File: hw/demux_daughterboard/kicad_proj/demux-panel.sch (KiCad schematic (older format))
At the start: 28 parts, among them P1 CONN_5, P10 CONN_2, P2 CONN_8X2, P3 CONN_8X2, P4 CONN_2, P5 CONN_5, P6 CONN_2, P7 CONN_8X2, P8 CONN_8X2, P9 CONN_3X2

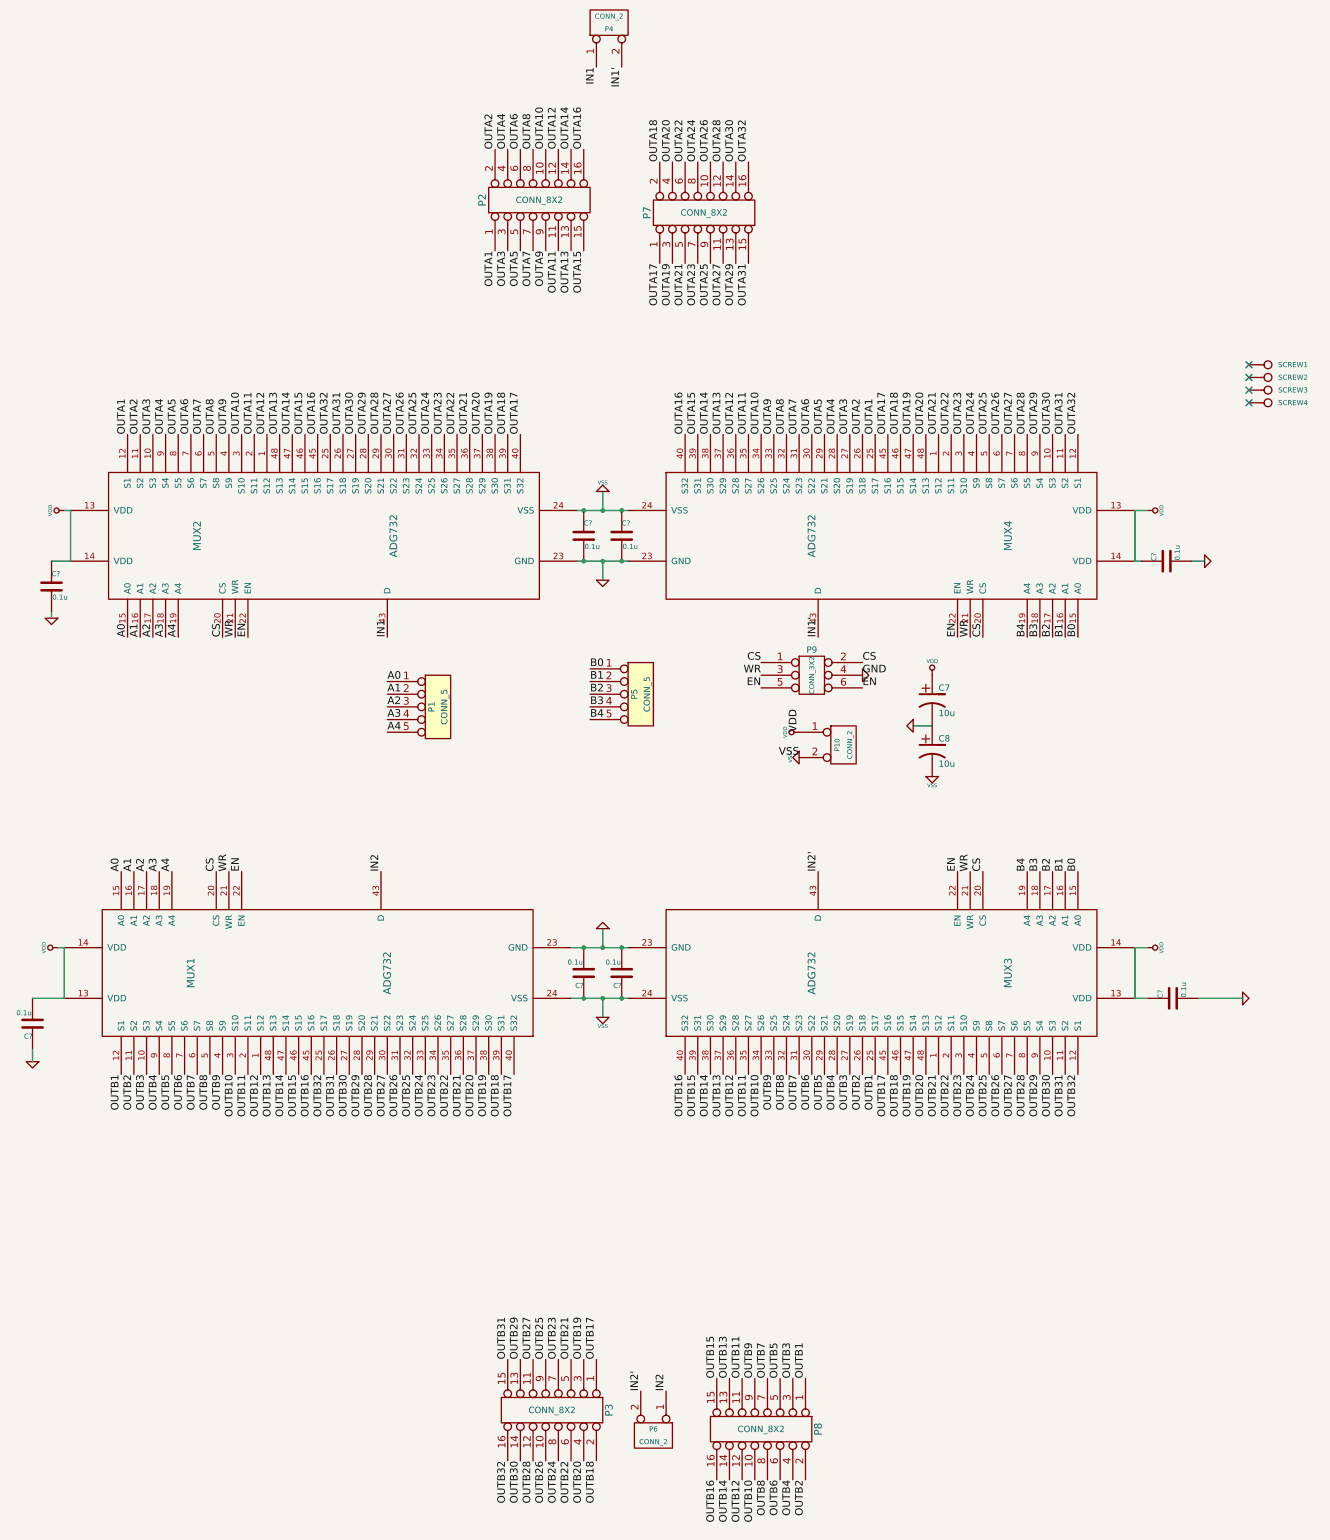
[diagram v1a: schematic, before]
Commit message: Finished daughterboard pcb with fusion pcb constraints, TODO: silkscreen
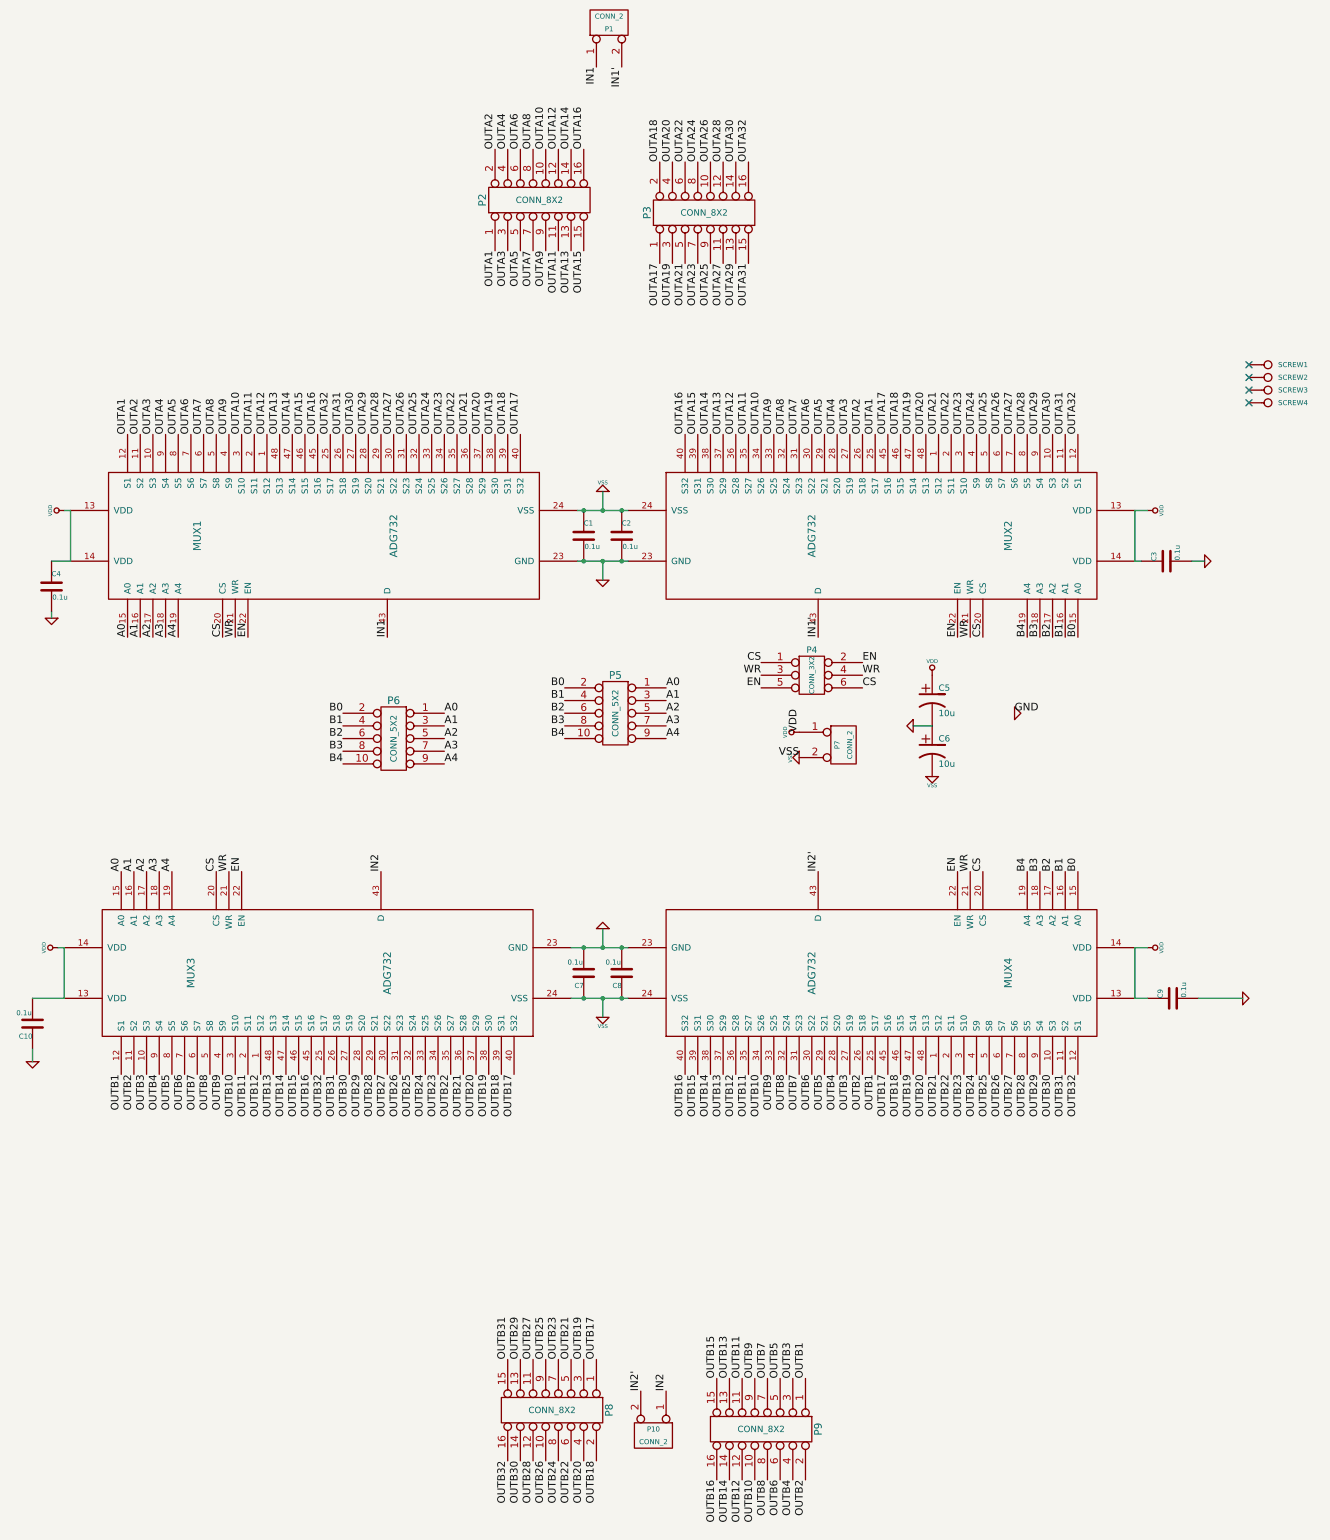
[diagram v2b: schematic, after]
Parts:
- removed P1, P5: CONN_5, symbol CONN_5
- added P5, P6: CONN_5X2, symbol CONN_5X2
- gave numbers to parts that had none: 8
- renumbered C7 to C5, C8 to C6, MUX2 to MUX1, MUX4 to MUX2, MUX1 to MUX3, MUX3 to MUX4, P4 to P1, P6 to P10, P7 to P3, P9 to P4, P10 to P7, P3 to P8, P8 to P9
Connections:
- net A0: now also P5.1, P6.1
- net A1: now also P5.3, P6.3
- net A2: now also P5.5, P6.5
- net A3: now also P5.7, P6.7
- net A4: now also P5.9, P6.9
- net B0: now also P5.2, P6.2
- net B1: now also P5.4, P6.4
- net B2: now also P5.6, P6.6
- net B3: now also P5.8, P6.8
- net B4: now also P5.10, P6.10
- net CS: now also P4.6; no longer P4.2
- net EN: now also P4.2; no longer P4.6
- net GND: no longer P4.4
- net WR: now also P4.4
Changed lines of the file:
@@
 LIBS:demuxcomplib
 LIBS:device
+LIBS:conn
 LIBS:demux-panel-cache
 EELAYER 24 0
@@
 Comment4 ""
 $EndDescr
-Text Label 5050 3150 0    60   ~ 0
+Text Label 3100 3500 2    60   ~ 0
 B0
 $Comp
@@
 $EndComp
 $Comp
-L CP1 C8
+L CP1 C6
 U 1 1 53239D33
 P 7750 3800
-F 0 "C8" H 7800 3900 50  0000 L CNN
+F 0 "C6" H 7800 3900 50  0000 L CNN
 F 1 "10u" H 7800 3700 50  0000 L CNN
 F 2 "" H 7750 3800 60  0001 C CNN
@@
 $EndComp
 $Comp
-L CP1 C7
+L CP1 C5
 U 1 1 53239D39
 P 7750 3400
-F 0 "C7" H 7800 3500 50  0000 L CNN
+F 0 "C5" H 7800 3500 50  0000 L CNN
 F 1 "10u" H 7800 3300 50  0000 L CNN
 F 2 "" H 7750 3400 60  0001 C CNN
@@
 L GND #PWR05
 U 1 1 53239D45
-P 7200 3200
-F 0 "#PWR05" H 7200 3200 30  0001 C CNN
-F 1 "GND" H 7200 3130 30  0001 C CNN
-F 2 "" H 7200 3200 60  0001 C CNN
-F 3 "" H 7200 3200 60  0001 C CNN
-	1    7200 3200
+P 8400 3500
+F 0 "#PWR05" H 8400 3500 30  0001 C CNN
+F 1 "GND" H 8400 3430 30  0001 C CNN
+F 2 "" H 8400 3500 60  0001 C CNN
+F 3 "" H 8400 3500 60  0001 C CNN
+	1    8400 3500
 	0    -1   -1   0
 $EndComp
@@
 	0    -1   -1   0
 $EndComp
-Text Label 7200 3200 0    60   ~ 0
+Text Label 8400 3500 0    60   ~ 0
 GND
 Text Label 6700 3850 2    60   ~ 0
@@
 Text Label 6400 3300 2    60   ~ 0
 EN
-Text Label 5050 3550 0    60   ~ 0
+Text Label 3100 3900 2    60   ~ 0
 B4
-Text Label 5050 3450 0    60   ~ 0
+Text Label 3100 3800 2    60   ~ 0
 B3
-Text Label 5050 3350 0    60   ~ 0
+Text Label 3100 3700 2    60   ~ 0
 B2
-Text Label 5050 3250 0    60   ~ 0
+Text Label 3100 3600 2    60   ~ 0
 B1
-Text Label 3450 3650 0    60   ~ 0
+Text Label 3900 3900 0    60   ~ 0
 A4
-Text Label 3450 3550 0    60   ~ 0
+Text Label 3900 3800 0    60   ~ 0
 A3
-Text Label 3450 3450 0    60   ~ 0
+Text Label 3900 3700 0    60   ~ 0
 A2
-Text Label 3450 3350 0    60   ~ 0
+Text Label 3900 3600 0    60   ~ 0
 A1
-Text Label 3450 3250 0    60   ~ 0
-A0
-$Comp
-L CONN_5 P5
-U 1 1 53239D66
-P 5450 3350
-F 0 "P5" V 5400 3350 50  0000 C CNN
-F 1 "CONN_5" V 5500 3350 50  0000 C CNN
-F 2 "" H 5450 3350 60  0001 C CNN
-F 3 "" H 5450 3350 60  0001 C CNN
-	1    5450 3350
-	1    0    0    -1
-$EndComp
-$Comp
-L CONN_5 P1
-U 1 1 53239D6C
-P 3850 3450
-F 0 "P1" V 3800 3450 50  0000 C CNN
-F 1 "CONN_5" V 3900 3450 50  0000 C CNN
-F 2 "" H 3850 3450 60  0001 C CNN
-F 3 "" H 3850 3450 60  0001 C CNN
-	1    3850 3450
-	1    0    0    -1
-$EndComp
 $Comp
 L CONN_1 SCREW4
@@
 $EndComp
 $Comp
-L ADG732 MUX1
+L ADG732 MUX3
 U 1 1 53239EC2
 P 2900 5550
-F 0 "MUX1" H 2900 6550 60  0000 C CNN
+F 0 "MUX3" H 2900 6550 60  0000 C CNN
 F 1 "ADG732" H 2900 5000 60  0000 C CNN
 F 2 "" H 2900 5550 60  0001 C CNN
@@
 $EndComp
 $Comp
-L ADG732 MUX2
+L ADG732 MUX1
 U 1 1 53239EC8
 P 2950 2100
-F 0 "MUX2" H 2950 3100 60  0000 C CNN
+F 0 "MUX1" H 2950 3100 60  0000 C CNN
 F 1 "ADG732" H 2950 1550 60  0000 C CNN
 F 2 "" H 2950 2100 60  0001 C CNN
@@
 $EndComp
 $Comp
-L ADG732 MUX4
+L ADG732 MUX2
 U 1 1 53239ECE
 P 7350 2100
-F 0 "MUX4" H 7350 3100 60  0000 C CNN
+F 0 "MUX2" H 7350 3100 60  0000 C CNN
 F 1 "ADG732" H 7350 1550 60  0000 C CNN
 F 2 "" H 7350 2100 60  0001 C CNN
@@
 $EndComp
 $Comp
-L CONN_3X2 P9
+L CONN_3X2 P4
 U 1 1 53239FB0
 P 6800 3250
-F 0 "P9" H 6800 3500 50  0000 C CNN
+F 0 "P4" H 6800 3500 50  0000 C CNN
 F 1 "CONN_3X2" V 6800 3300 40  0000 C CNN
 F 2 "" H 6800 3250 60  0000 C CNN
@@
 	1    0    0    -1
 $EndComp
+Text Label 7200 3300 0    60   ~ 0
+CS
 Text Label 7200 3100 0    60   ~ 0
-CS
-Text Label 7200 3300 0    60   ~ 0
 EN
 $Comp
-L CONN_2 P10
+L CONN_2 P7
 U 1 1 53239FDE
 P 7050 3750
-F 0 "P10" V 7000 3750 40  0000 C CNN
+F 0 "P7" V 7000 3750 40  0000 C CNN
 F 1 "CONN_2" V 7100 3750 40  0000 C CNN
 F 2 "" H 7050 3750 60  0000 C CNN
@@
 $EndComp
 $Comp
-L CONN_8X2 P7
+L CONN_8X2 P3
 U 1 1 5323C0BE
 P 5950 -450
-F 0 "P7" H 5950 0   60  0000 C CNN
+F 0 "P3" H 5950 0   60  0000 C CNN
 F 1 "CONN_8X2" V 5950 -450 50  0000 C CNN
 F 2 "" H 5950 -450 60  0000 C CNN
@@
 OUTA32
 $Comp
-L CONN_2 P4
+L CONN_2 P1
 U 1 1 5323C58F
 P 5200 -1950
-F 0 "P4" V 5150 -1950 40  0000 C CNN
+F 0 "P1" V 5150 -1950 40  0000 C CNN
 F 1 "CONN_2" V 5250 -1950 40  0000 C CNN
 F 2 "" H 5200 -1950 60  0000 C CNN
@@
 IN1'
 $Comp
-L CONN_8X2 P8
+L CONN_8X2 P9
 U 1 1 5323C6F0
 P 6400 9150
-F 0 "P8" H 6400 9600 60  0000 C CNN
+F 0 "P9" H 6400 9600 60  0000 C CNN
 F 1 "CONN_8X2" V 6400 9150 50  0000 C CNN
 F 2 "" H 6400 9150 60  0000 C CNN
@@
 $EndComp
 $Comp
-L CONN_8X2 P3
+L CONN_8X2 P8
 U 1 1 5323C6F6
 P 4750 9000
-F 0 "P3" H 4750 9450 60  0000 C CNN
+F 0 "P8" H 4750 9450 60  0000 C CNN
 F 1 "CONN_8X2" V 4750 9000 50  0000 C CNN
 F 2 "" H 4750 9000 60  0000 C CNN
@@
 OUTB16
 $Comp
-L CONN_2 P6
+L CONN_2 P10
 U 1 1 5323C787
 P 5550 9200
-F 0 "P6" V 5500 9200 40  0000 C CNN
+F 0 "P10" V 5500 9200 40  0000 C CNN
 F 1 "CONN_2" V 5600 9200 40  0000 C CNN
 F 2 "" H 5550 9200 60  0000 C CNN
@@
 Connection ~ 5000 5750
 $Comp
-L ADG732 MUX3
+L ADG732 MUX4
 U 1 1 53239EBC
 P 7350 5550
-F 0 "MUX3" H 7350 6550 60  0000 C CNN
+F 0 "MUX4" H 7350 6550 60  0000 C CNN
 F 1 "ADG732" H 7350 5000 60  0000 C CNN
 F 2 "" H 7350 5550 60  0001 C CNN
@@
 	650  6150 650  6250
 $Comp
-L C C?
+L C C1
 U 1 1 5323D5A7
 P 5000 2100
-F 0 "C?" H 5000 2200 40  0000 L CNN
+F 0 "C1" H 5000 2200 40  0000 L CNN
 F 1 "0.1u" H 5006 2015 40  0000 L CNN
 F 2 "" H 5038 1950 30  0000 C CNN
@@
 $EndComp
 $Comp
-L C C?
+L C C2
 U 1 1 5323D5D2
 P 5300 2100
-F 0 "C?" H 5300 2200 40  0000 L CNN
+F 0 "C2" H 5300 2200 40  0000 L CNN
 F 1 "0.1u" H 5306 2015 40  0000 L CNN
 F 2 "" H 5338 1950 30  0000 C CNN
@@
 $EndComp
 $Comp
-L C C?
+L C C4
 U 1 1 5323D5D8
 P 800 2500
-F 0 "C?" H 800 2600 40  0000 L CNN
+F 0 "C4" H 800 2600 40  0000 L CNN
 F 1 "0.1u" H 806 2415 40  0000 L CNN
 F 2 "" H 838 2350 30  0000 C CNN
@@
 $EndComp
 $Comp
-L C C?
+L C C3
 U 1 1 5323D5E8
 P 9600 2300
-F 0 "C?" H 9600 2400 40  0000 L CNN
+F 0 "C3" H 9600 2400 40  0000 L CNN
 F 1 "0.1u" H 9606 2215 40  0000 L CNN
 F 2 "" H 9638 2150 30  0000 C CNN
@@
 $EndComp
 $Comp
-L C C?
+L C C9
 U 1 1 5323D5F8
 P 9650 5750
-F 0 "C?" H 9650 5850 40  0000 L CNN
+F 0 "C9" H 9650 5850 40  0000 L CNN
 F 1 "0.1u" H 9656 5665 40  0000 L CNN
 F 2 "" H 9688 5600 30  0000 C CNN
@@
 $EndComp
 $Comp
-L C C?
+L C C7
 U 1 1 5323D608
 P 5000 5550
-F 0 "C?" H 5000 5650 40  0000 L CNN
+F 0 "C7" H 5000 5650 40  0000 L CNN
 F 1 "0.1u" H 5006 5465 40  0000 L CNN
 F 2 "" H 5038 5400 30  0000 C CNN
@@
 $EndComp
 $Comp
-L C C?
+L C C8
 U 1 1 5323D615
 P 5300 5550
-F 0 "C?" H 5300 5650 40  0000 L CNN
+F 0 "C8" H 5300 5650 40  0000 L CNN
 F 1 "0.1u" H 5306 5465 40  0000 L CNN
 F 2 "" H 5338 5400 30  0000 C CNN
@@
 $EndComp
 $Comp
-L C C?
+L C C10
 U 1 1 5323D61B
 P 650 5950
-F 0 "C?" H 650 6050 40  0000 L CNN
+F 0 "C10" H 650 6050 40  0000 L CNN
 F 1 "0.1u" H 656 5865 40  0000 L CNN
 F 2 "" H 688 5800 30  0000 C CNN
@@
 	-1   0    0    1
 $EndComp
+Text Label 7200 3200 0    60   ~ 0
+WR
+$Comp
+L CONN_5X2 P6
+U 1 1 53250D68
+P 3500 3700
+F 0 "P6" H 3500 4000 60  0000 C CNN
+F 1 "CONN_5X2" V 3500 3700 50  0000 C CNN
+F 2 "" H 3500 3700 60  0000 C CNN
+F 3 "" H 3500 3700 60  0000 C CNN
+	1    3500 3700
+	-1   0    0    -1
+$EndComp
+Text Label 3900 3500 0    60   ~ 0
+A0
+Text Label 4850 3300 2    60   ~ 0
+B0
+Text Label 4850 3700 2    60   ~ 0
+B4
+Text Label 4850 3600 2    60   ~ 0
+B3
+Text Label 4850 3500 2    60   ~ 0
+B2
+Text Label 4850 3400 2    60   ~ 0
+B1
+Text Label 5650 3700 0    60   ~ 0
+A4
+Text Label 5650 3600 0    60   ~ 0
+A3
+Text Label 5650 3500 0    60   ~ 0
+A2
+Text Label 5650 3400 0    60   ~ 0
+A1
+$Comp
+L CONN_5X2 P5
+U 1 1 53250D98
+P 5250 3500
+F 0 "P5" H 5250 3800 60  0000 C CNN
+F 1 "CONN_5X2" V 5250 3500 50  0000 C CNN
+F 2 "" H 5250 3500 60  0000 C CNN
+F 3 "" H 5250 3500 60  0000 C CNN
+	1    5250 3500
+	-1   0    0    -1
+$EndComp
+Text Label 5650 3300 0    60   ~ 0
+A0
 $EndSCHEMATC
